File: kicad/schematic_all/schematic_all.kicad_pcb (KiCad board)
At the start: 2 copper layers, 88.9 x 88.9 mm, 42 parts, among them J1 Power In, SW1 Button 1, SW2 Encoder 1, SW3 Button 2, SW4 Encoder 2, SW5 Button 3, U1 L7805, U2 RPi_Pico, U3 RDA5807M_Module, U4 LM386

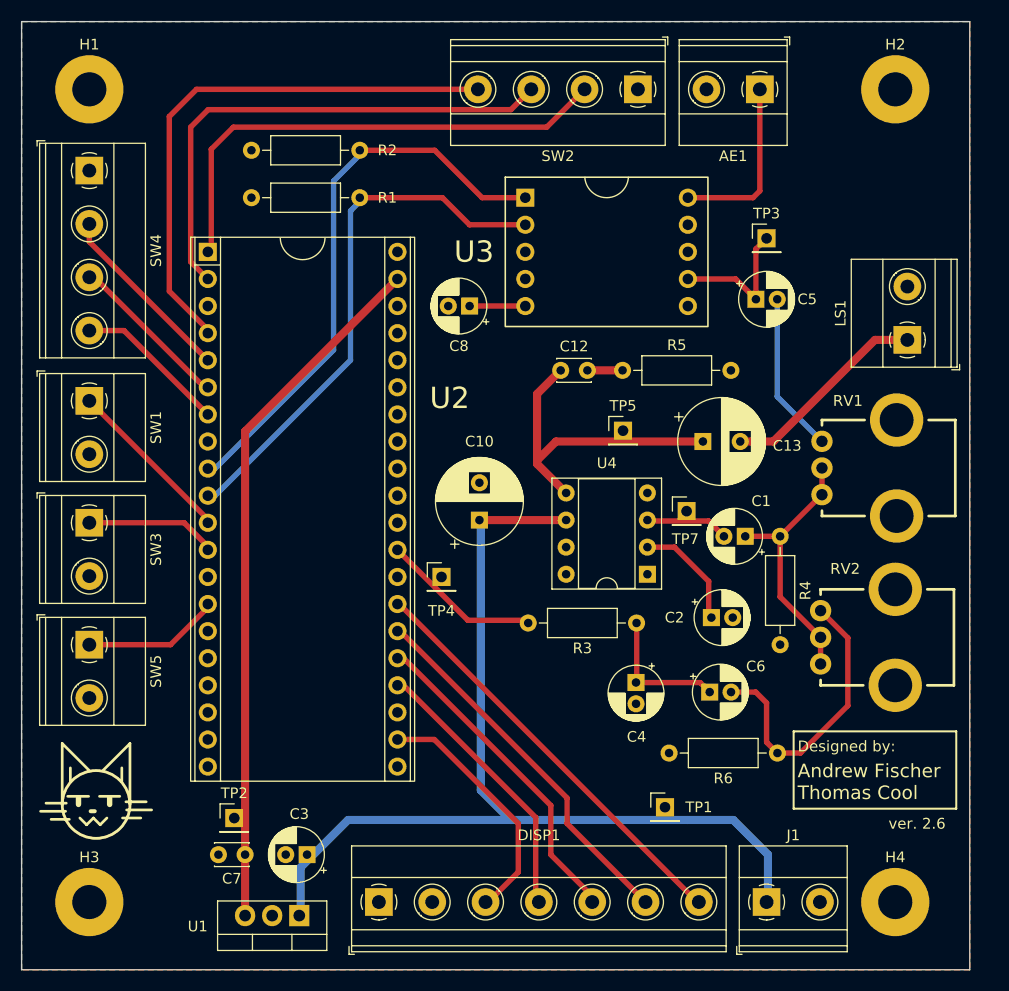
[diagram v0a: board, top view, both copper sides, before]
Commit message: full board check
replace incorrect radial cap with disc
change capacitor values around amp
add jack labels
reground pot chassis
tweak positions
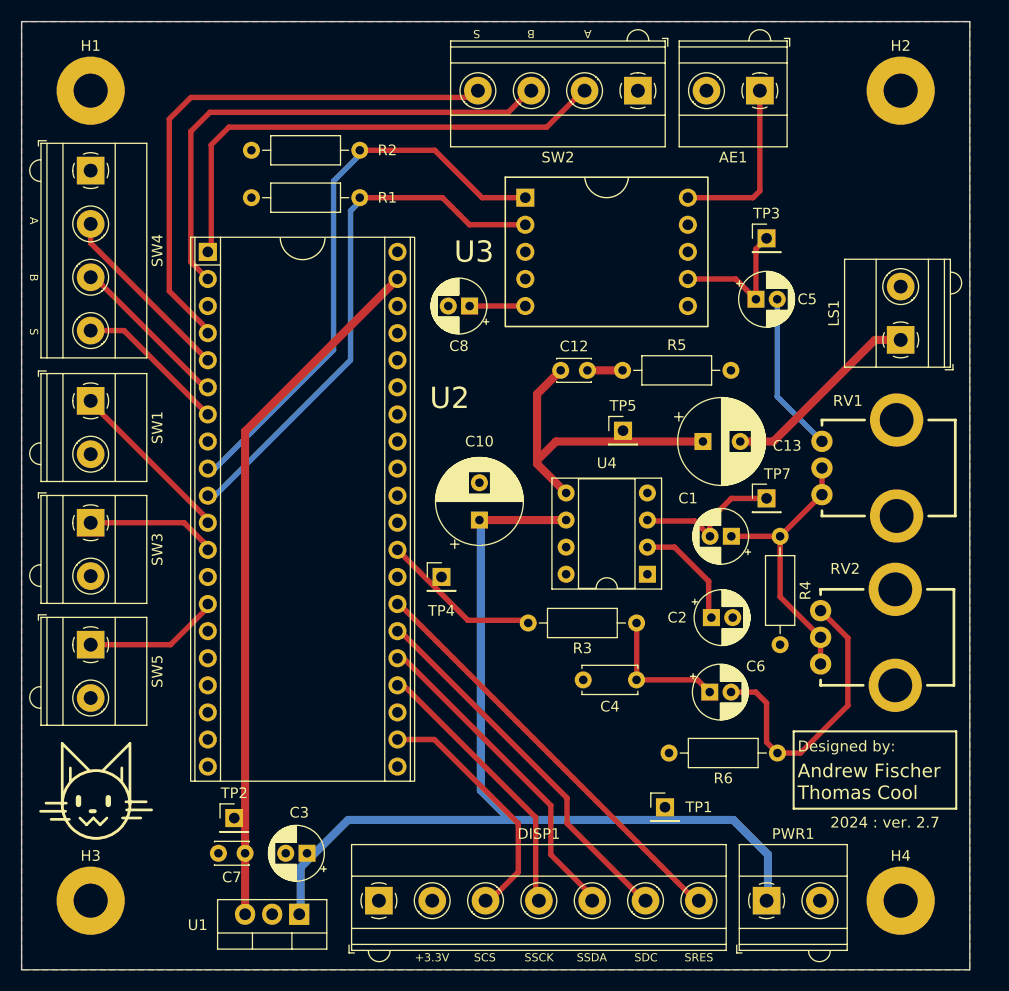
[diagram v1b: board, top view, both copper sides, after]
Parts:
- C1, C2: value 220nF -> 100uF
- C4: footprint Capacitor_THT:CP_Radial_D5.0mm_P2.00mm -> Capacitor_THT:C_Disc_D5.0mm_W2.5mm_P5.00mm
- moved TP7 7.59 mm to (127.0, 82.8)
- moved C1 1.30 mm to (123.7, 86.4)
- moved LS1 0.63 mm to (139.6, 67.9)
- moved H4 0.52 mm to (139.6, 120.5)
- moved H2 0.52 mm to (139.6, 44.6)
- moved C4 0.25 mm to (114.8, 99.8), turned to 180 degrees
- moved H3 0.18 mm to (63.6, 120.5)
- moved H1 0.18 mm to (63.6, 44.6)
- moved DISP1 0.13 mm to (90.7, 120.5)
- moved PWR1 0.13 mm to (127.0, 120.5)
- moved SW1 0.13 mm to (63.6, 73.7)
- moved SW3 0.13 mm to (63.6, 85.1)
- moved SW4 0.13 mm to (63.6, 52.1)
- moved SW5 0.13 mm to (63.6, 96.5)
- moved AE1 0.13 mm to (126.4, 44.6)
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- renumbered J1 to PWR1
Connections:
- RV1 pad 4: (no net) -> GND
- RV1 pad 5: (no net) -> GND
- RV2 pad 4: (no net) -> GND
- RV2 pad 5: (no net) -> GND
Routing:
- net Net-(U4-+): track 7.81 -> 14.2 mm
- net Net-(C1-Pad1): track 24.9 -> 26.2 mm
- net Net-(C13-Pad2): track 19.6 -> 19.0 mm
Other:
- board text added: "+3.3V"
- board text added: "2024 : ver. 2.7"
- board text added: "A"
- board text added: "B"
- board text added: "S"
- board text added: "SCS"
- board text added: "SDC"
- board text added: "SRES"
- board text added: "SSCK"
- board text added: "SSDA"
- board text removed: "ver. 2.6"

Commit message: Fixed U3 Pad 5 3.3V connection
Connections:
- U3 pad 5: +3.3V -> Bypass-Pin5
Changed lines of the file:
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@@
 	(net 51 "+12V")
 	(net 52 "unconnected-(U2-ADC_VREF-Pad35)")
+	(net 53 "Bypass-Pin5")
 	(footprint "Connector_PinHeader_2.54mm:PinHeader_1x01_P2.54mm_Vertical"
 		(layer "F.Cu")
@@
 			(layers "*.Cu" "*.Mask")
 			(remove_unused_layers no)
-			(net 4 "+3.3V")
+			(net 53 "Bypass-Pin5")
 			(pinfunction "VDD")
 			(pintype "power_in")
@@
 		(tags "C Disc series Radial pin pitch 5.00mm  diameter 5mm width 2.5mm Capacitor")
 		(property "Reference" "C4"
-			(at 2.5 -2.5 360)
+			(at 2.5 -2.5 0)
 			(layer "F.SilkS")
 			(effects
@@
 		)
 		(property "Value" "1nF"
-			(at 2.5 2.5 360)
+			(at 2.5 2.5 0)
 			(layer "F.Fab")
 			(effects
@@
 		)
 		(fp_text user "${REFERENCE}"
-			(at 2.5 0 360)
+			(at 2.5 0 0)
 			(layer "F.Fab")
 			(effects

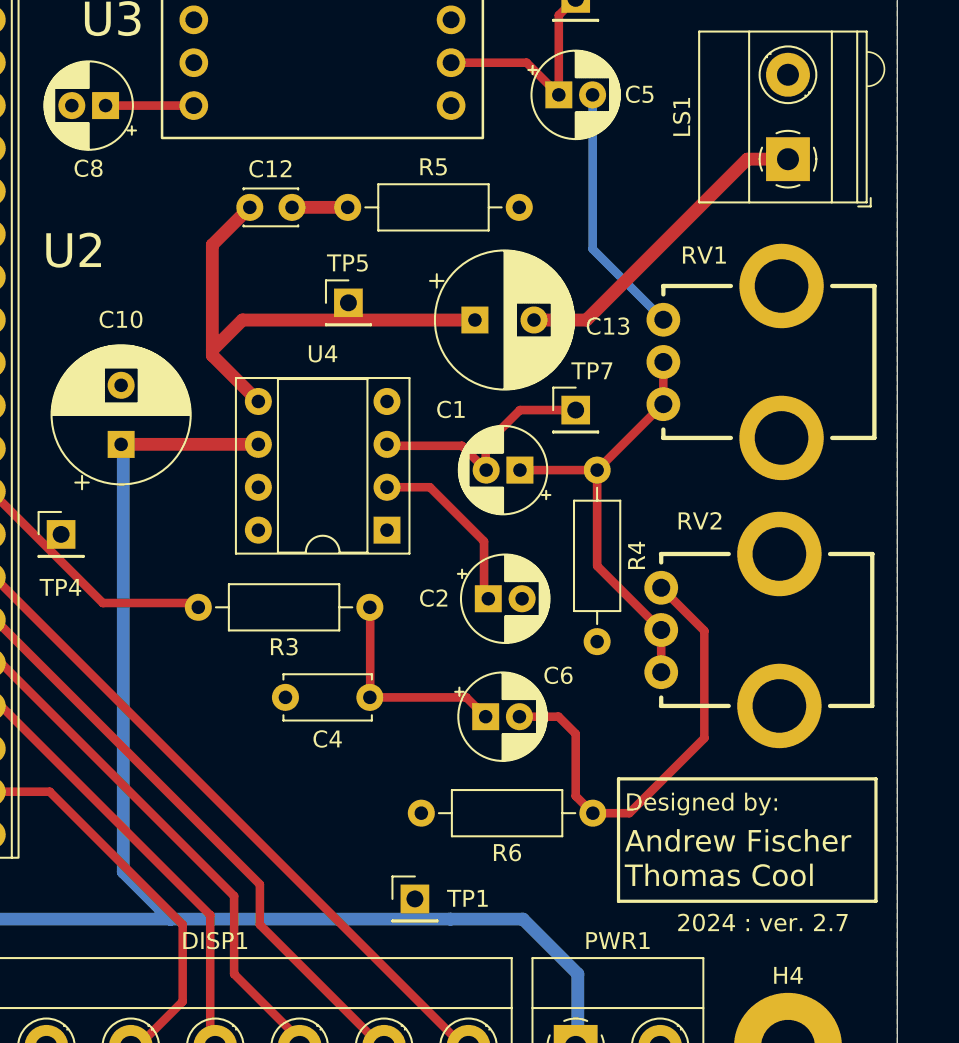
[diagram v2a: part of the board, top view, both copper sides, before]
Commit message: Isolated C8 and U3 pin 5 track
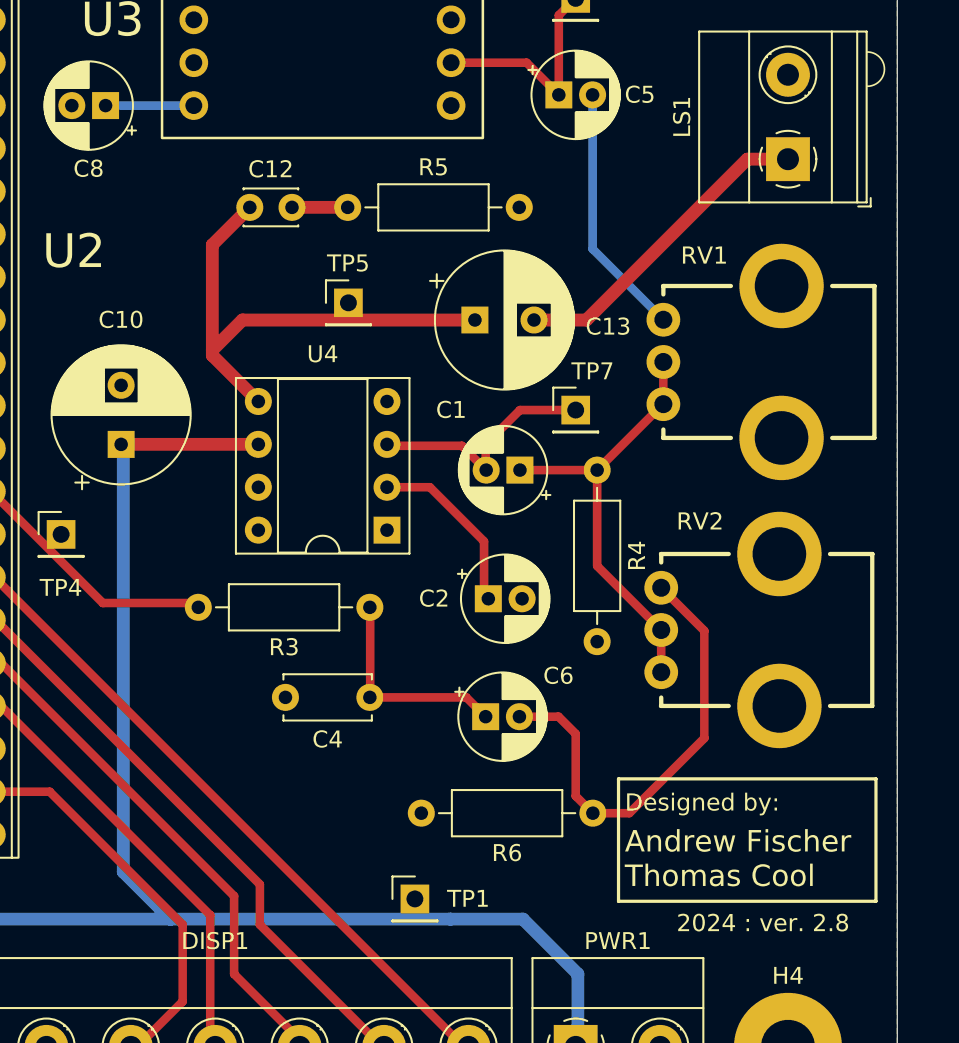
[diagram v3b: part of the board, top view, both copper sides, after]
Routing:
- net Bypass-Pin5: track 0.00 -> 5.22 mm
- net +3.3V: track 5.22 -> 0.00 mm
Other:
- board text added: "2024 : ver. 2.8"
- board text removed: "2024 : ver. 2.7"
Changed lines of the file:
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@@
 		)
 	)
-	(gr_text "2024 : ver. 2.7"
+	(gr_text "2024 : ver. 2.8"
 		(at 132.969 113.792 0)
 		(layer "F.SilkS")
@@
 		(layer "F.Cu")
 		(net 3)
-	)
-	(segment
-		(start 104.38 64.77)
-		(end 99.155 64.77)
-		(width 0.508)
-		(layer "F.Cu")
-		(net 4)
 	)
 	(segment
@@
 		(net 51)
 	)
+	(segment
+		(start 104.38 64.77)
+		(end 99.155 64.77)
+		(width 0.508)
+		(layer "B.Cu")
+		(net 53)
+	)
 	(zone

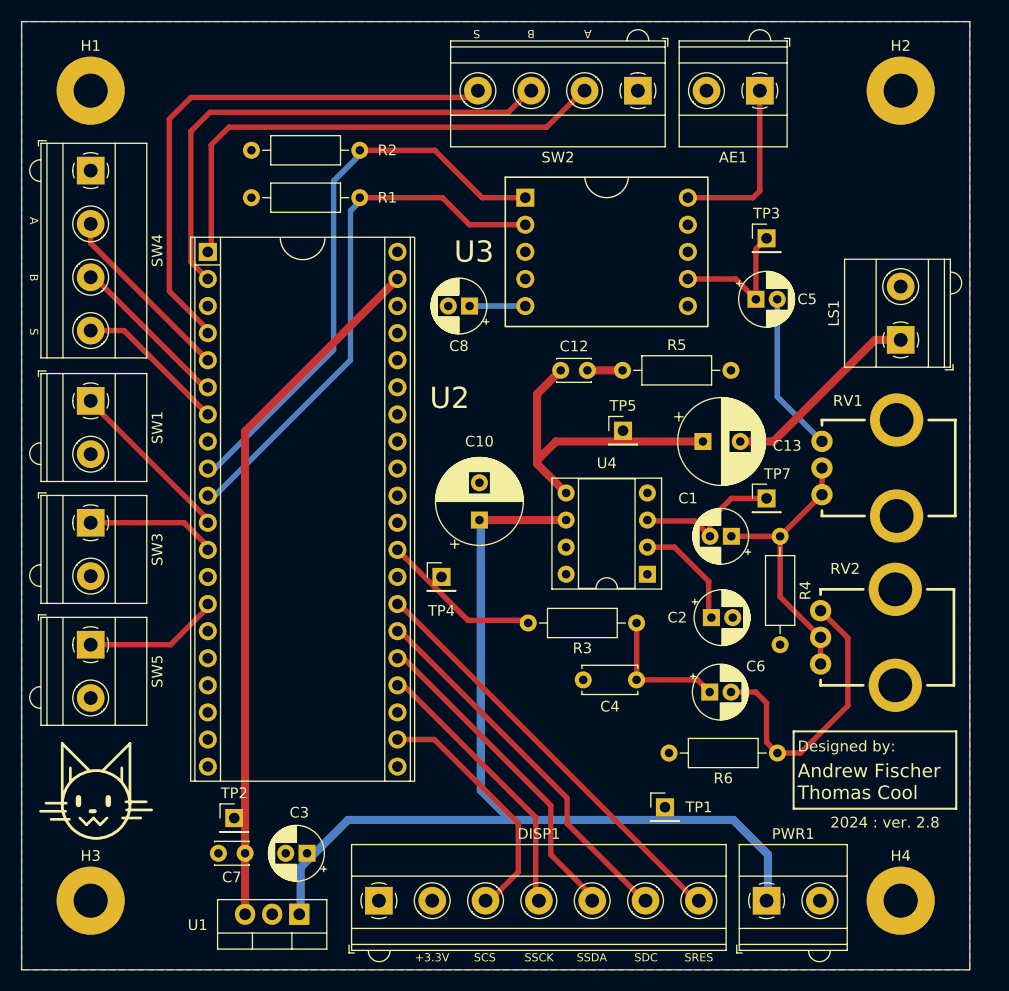
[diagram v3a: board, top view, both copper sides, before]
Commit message: unpolarize amp coupling capacitors
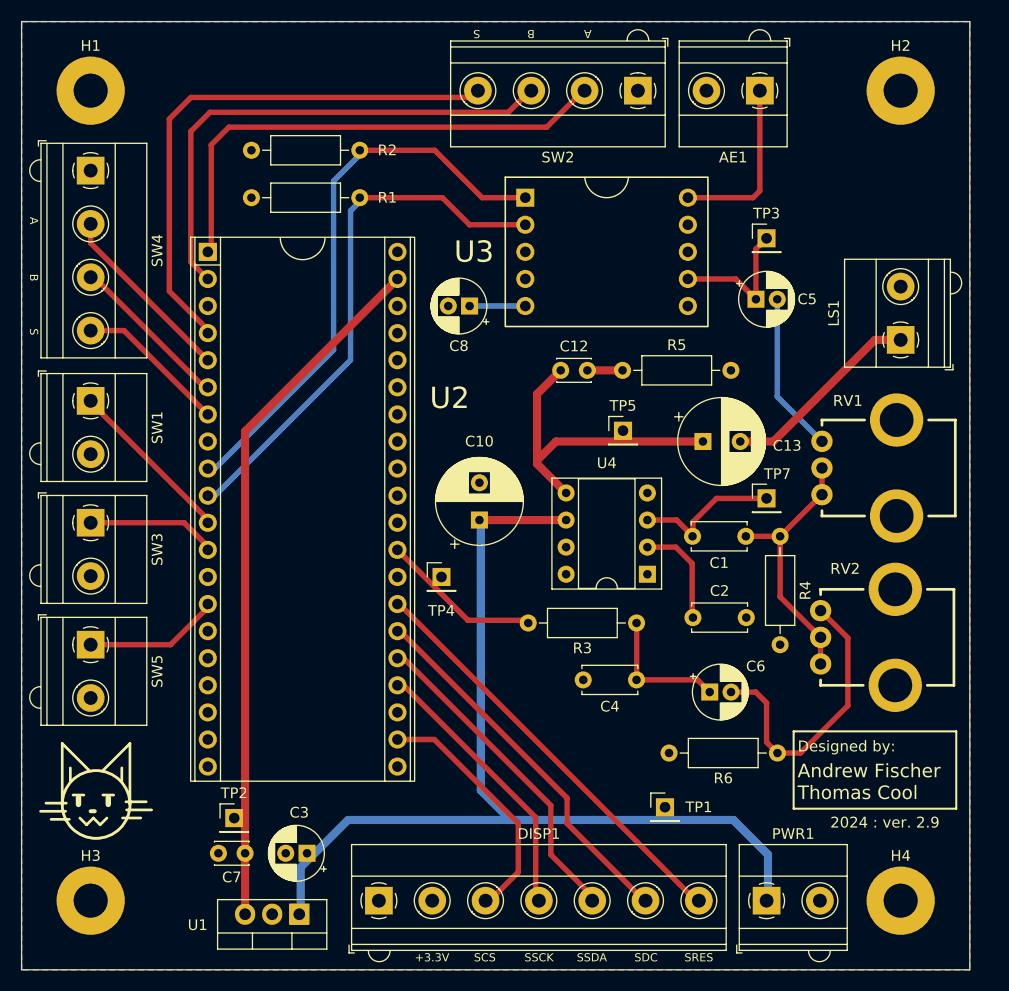
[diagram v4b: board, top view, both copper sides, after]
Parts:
- C1, C2: value 100uF -> 220nF; footprint Capacitor_THT:CP_Radial_D5.0mm_P2.00mm -> Capacitor_THT:C_Disc_D5.0mm_W2.5mm_P5.00mm
- moved C2 1.73 mm to (120.1, 94.0)
- moved C1 1.36 mm to (125.1, 86.4)
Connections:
- RV1 pad 4: GND -> (no net)
- RV1 pad 5: GND -> (no net)
- RV2 pad 4: GND -> (no net)
- RV2 pad 5: GND -> (no net)
- U3 pad 5: Bypass-Pin5 -> +3.3V
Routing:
- net Bypass-Pin5: track 5.22 -> 0.00 mm
- net +3.3V: track 0.00 -> 5.22 mm
- net Net-(C1-Pad1): track 26.2 -> 24.9 mm
- net Net-(U4--): track 10.5 -> 9.94 mm
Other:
- board text added: "2024 : ver. 2.9"
- board text removed: "2024 : ver. 2.8"

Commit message: Minor changes
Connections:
- U3 pad 5: +3.3V -> 3.3V-Decouple
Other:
- board text added: "2024 : ver. 3.0"
- board text removed: "2024 : ver. 2.9"
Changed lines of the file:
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@@
 	(net 51 "+12V")
 	(net 52 "unconnected-(U2-ADC_VREF-Pad35)")
+	(net 53 "3.3V-Decouple")
 	(footprint "Connector_PinHeader_2.54mm:PinHeader_1x01_P2.54mm_Vertical"
 		(layer "F.Cu")
@@
 			(layers "*.Cu" "*.Mask")
 			(remove_unused_layers no)
-			(net 4 "+3.3V")
+			(net 53 "3.3V-Decouple")
 			(pinfunction "VDD")
 			(pintype "power_in")
@@
 		)
 	)
-	(gr_text "2024 : ver. 2.9"
+	(gr_text "2024 : ver. 3.0"
 		(at 132.969 113.792 0)
 		(layer "F.SilkS")

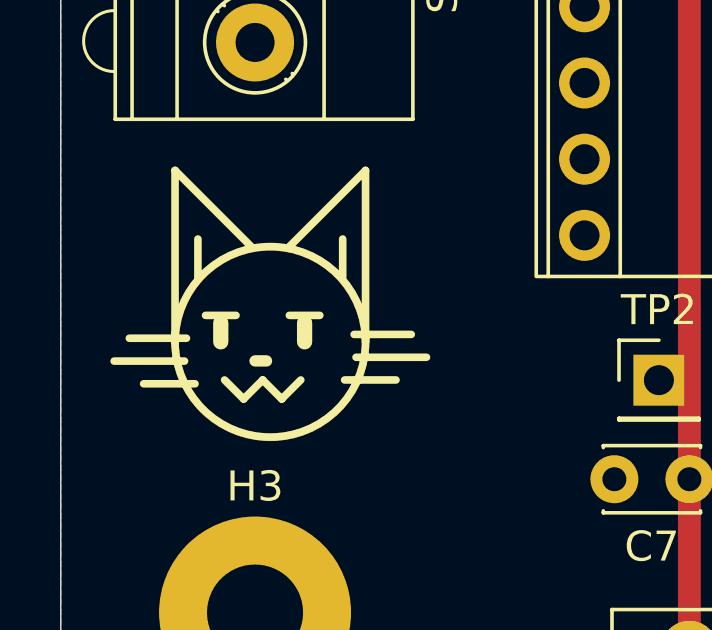
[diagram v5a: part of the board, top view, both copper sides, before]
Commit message: remove fill zone around U3 pin 5
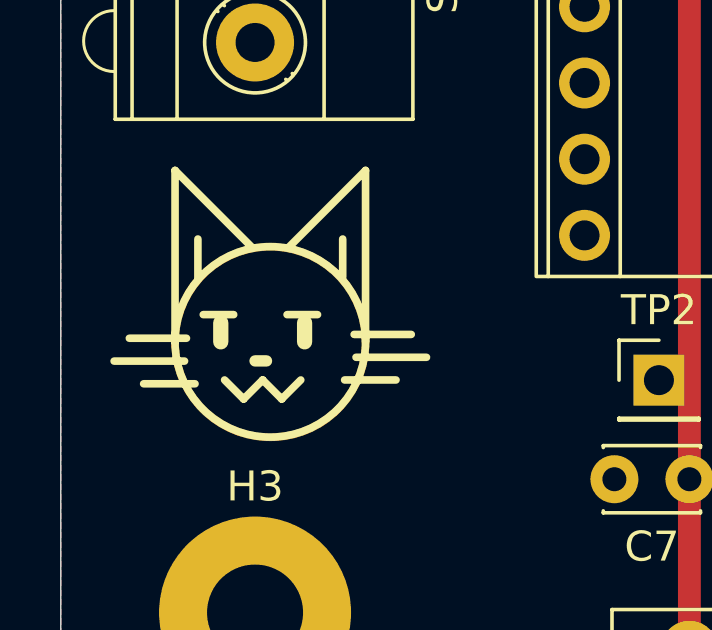
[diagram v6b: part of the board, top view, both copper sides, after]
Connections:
- U3 pad 5: 3.3V-Decouple -> +3.3V
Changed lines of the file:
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@@
 		(0 "F.Cu" signal)
 		(31 "B.Cu" signal)
-		(32 "B.Adhes" user "B.Adhesive")
-		(33 "F.Adhes" user "F.Adhesive")
-		(34 "B.Paste" user)
-		(35 "F.Paste" user)
 		(36 "B.SilkS" user "B.Silkscreen")
 		(37 "F.SilkS" user "F.Silkscreen")
@@
 		(40 "Dwgs.User" user "User.Drawings")
 		(41 "Cmts.User" user "User.Comments")
-		(42 "Eco1.User" user "User.Eco1")
-		(43 "Eco2.User" user "User.Eco2")
 		(44 "Edge.Cuts" user)
 		(45 "Margin" user)
@@
 		(48 "B.Fab" user)
 		(49 "F.Fab" user)
-		(50 "User.1" user)
-		(51 "User.2" user)
-		(52 "User.3" user)
-		(53 "User.4" user)
-		(54 "User.5" user)
-		(55 "User.6" user)
-		(56 "User.7" user)
-		(57 "User.8" user)
-		(58 "User.9" user)
 	)
 	(setup
@@
 	(net 51 "+12V")
 	(net 52 "unconnected-(U2-ADC_VREF-Pad35)")
-	(net 53 "3.3V-Decouple")
 	(footprint "Connector_PinHeader_2.54mm:PinHeader_1x01_P2.54mm_Vertical"
 		(layer "F.Cu")
@@
 			(layers "*.Cu" "*.Mask")
 			(remove_unused_layers no)
-			(net 53 "3.3V-Decouple")
+			(net 4 "+3.3V")
 			(pinfunction "VDD")
 			(pintype "power_in")
@@
 	)
 	(gr_line
-		(start 64.77 110.617)
-		(end 65.786 110.617)
+		(start 64.6938 110.5916)
+		(end 65.7098 110.5916)
 		(stroke
 			(width 0.254)
@@
 	)
 	(gr_line
-		(start 61.976 110.617)
-		(end 62.992 110.617)
+		(start 61.8998 110.5916)
+		(end 62.9158 110.5916)
 		(stroke
 			(width 0.254)
@@
 	)
 	(zone
+		(net 0)
+		(net_name "")
+		(layer "F.Cu")
+		(hatch edge 0.5)
+		(connect_pads
+			(clearance 0)
+		)
+		(min_thickness 0.25)
+		(filled_areas_thickness no)
+		(keepout
+			(tracks allowed)
+			(vias allowed)
+			(pads allowed)
+			(copperpour not_allowed)
+			(footprints allowed)
+		)
+		(fill
+			(thermal_gap 0.5)
+			(thermal_bridge_width 0.5)
+		)
+		(polygon
+			(pts
+				(xy 103.2764 65.532) (xy 103.632 65.8876) (xy 105.1306 65.8876) (xy 105.4862 65.532) (xy 105.4862 64.008)
+				(xy 105.1306 63.6524) (xy 103.632 63.6524) (xy 103.2764 64.008)
+			)
+		)
+	)
+	(zone
